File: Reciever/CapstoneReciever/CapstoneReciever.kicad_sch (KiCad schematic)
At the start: 70 parts, among them J1 Conn_01x04, J2 Conn_01x04, J3 Sol1Conn, J4 Sol2Conn, J5 Sol3Conn, J6 Sol4Conn, Q1 CSD18502Q5B, Q2 CSD18502Q5B, Q3 CSD18540Q5B, Q4 CSD18540Q5B, Q5 CSD18540Q5B, Q6 CSD18540Q5B, U1 LM73606RNPR, U2 TPS552882RPMR, U3 ESP32-WROOM-32UE

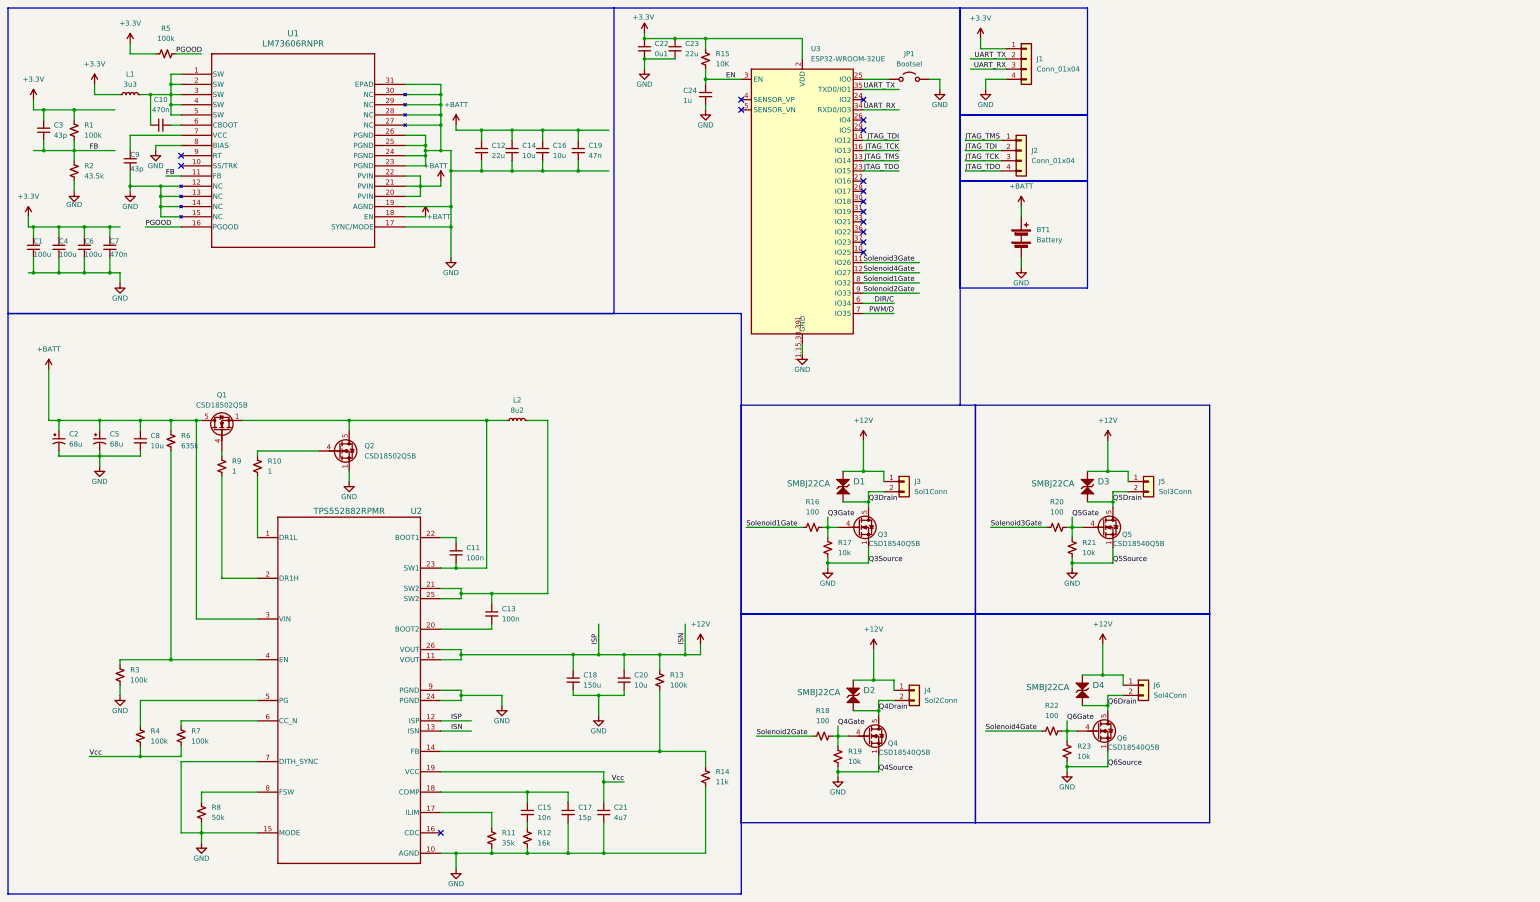
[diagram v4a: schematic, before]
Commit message: Removed convoluted battery power routing in exchange of DIN mounted AC-DC converter and DC-DC converter inputs
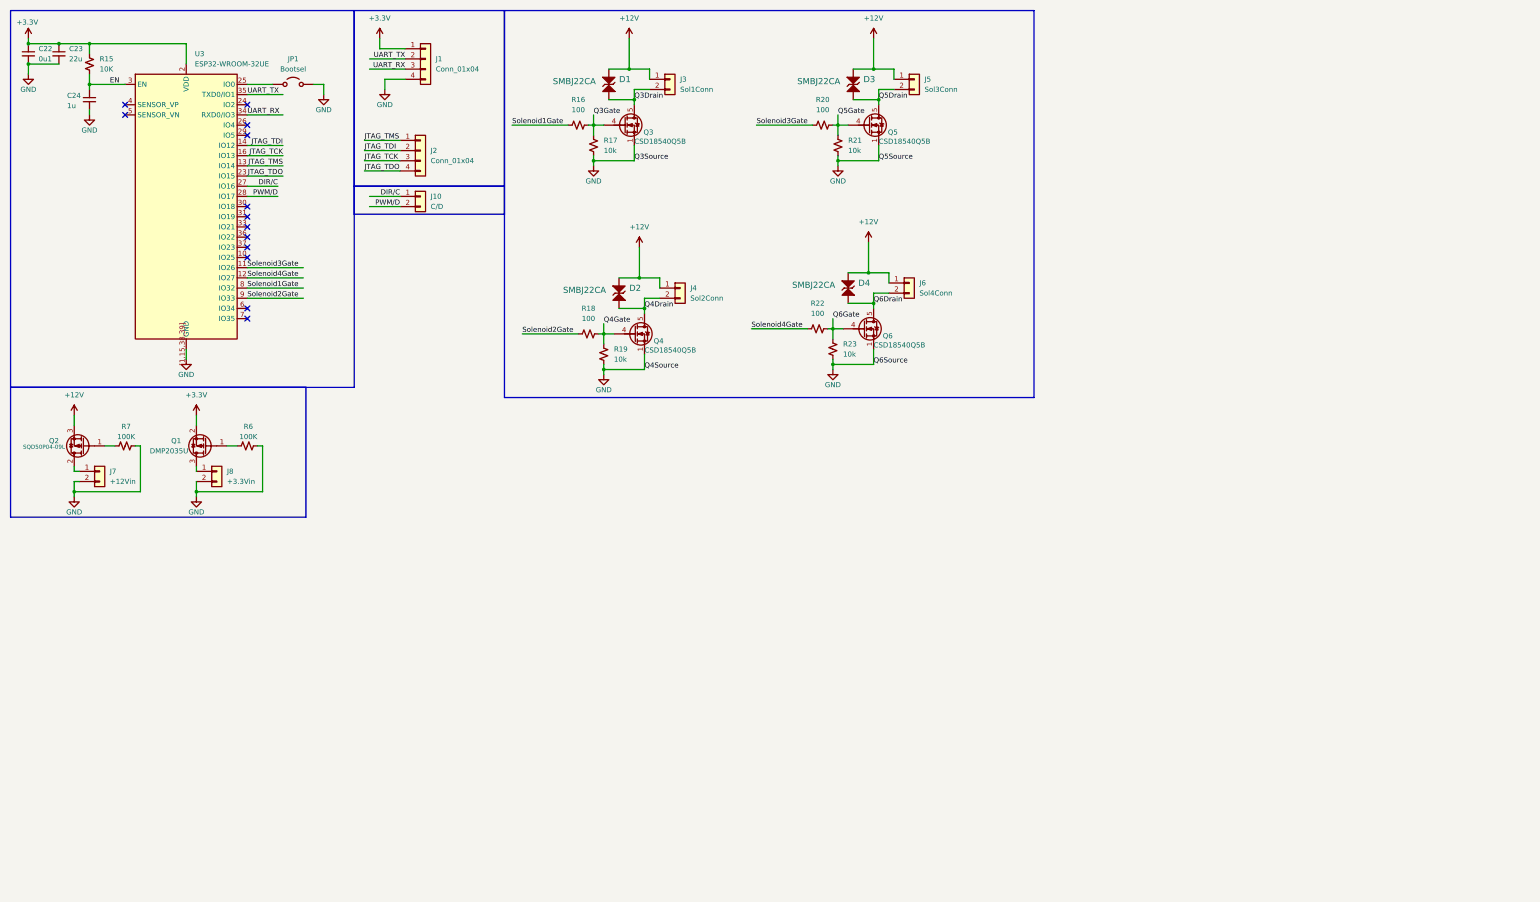
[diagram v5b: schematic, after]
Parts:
- removed BT1: Battery, TerminalBlock_CUI:TerminalBlock_CUI_TB007-508-02_1x02_P5.08mm_Horizontal, symbol Device:Battery
- removed C1, C4, C6: 100u, Capacitor_SMD:C_0603_1608Metric, symbol Device:C_Small
- removed C10, C7: 470n, Capacitor_SMD:C_0402_1005Metric, symbol Device:C_Small
- removed C11, C13: 100n, Capacitor_SMD:C_0402_1005Metric, symbol Device:C_Small
- removed C12: 22u, Capacitor_SMD:C_0603_1608Metric, symbol Device:C_Small
- removed C14, C16, C20, C8: 10u, Capacitor_SMD:C_0603_1608Metric, symbol Device:C_Small
- removed C15: 10n, Capacitor_SMD:C_0402_1005Metric, symbol Device:C_Small
- removed C17: 15p, Capacitor_SMD:C_0402_1005Metric, symbol Device:C_Small
- removed C18: 150u, Capacitor_SMD:C_0603_1608Metric, symbol Device:C_Small
- removed C19: 47n, Capacitor_SMD:C_0402_1005Metric, symbol Device:C_Small
- removed C2, C5: 68u, Capacitor_SMD:C_0603_1608Metric, symbol Device:C_Polarized_Small_US
- removed C21: 4u7, Capacitor_SMD:C_0603_1608Metric, symbol Device:C_Small
- removed C3, C9: 43p, Capacitor_SMD:C_0402_1005Metric, symbol Device:C_Small
- removed L1: 3u3, Capacitor_SMD:C_0603_1608Metric, symbol Device:L_Small
- removed L2: 8u2, Capacitor_SMD:C_0603_1608Metric, symbol Device:L_Small
- removed Q1, Q2: CSD18502Q5B, Package_TO_SOT_SMD:TDSON-8-1, symbol Transistor_FET:CSD18502Q5B
- removed R1, R13, R3, R4, R5: 100k, Resistor_SMD:R_0603_1608Metric, symbol Device:R_Small_US
- removed R10, R9: 1, Resistor_SMD:R_0603_1608Metric, symbol Device:R_Small_US
- removed R11: 35k, Resistor_SMD:R_0603_1608Metric, symbol Device:R_Small_US
- removed R12: 16k, Resistor_SMD:R_0603_1608Metric, symbol Device:R_Small_US
- removed R14: 11k, Resistor_SMD:R_0603_1608Metric, symbol Device:R_Small_US
- removed R2: 43.5k, Resistor_SMD:R_0603_1608Metric, symbol Device:R_Small_US
- removed R8: 50k, Resistor_SMD:R_0603_1608Metric, symbol Device:R_Small_US
- removed U1: LM73606RNPR, footprints2:RNP30_TEX, symbol LM73606:LM73606RNPR
- removed U2: TPS552882RPMR, footprints2:RPM0026A-MFG, symbol TPS552882RPMR:TPS552882RPMR
- added J10: C/D, TerminalBlock_CUI:TerminalBlock_CUI_TB007-508-02_1x02_P5.08mm_Horizontal, symbol Connector_Generic:Conn_01x02
- added J7: +12Vin, TerminalBlock_CUI:TerminalBlock_CUI_TB007-508-02_1x02_P5.08mm_Horizontal, symbol Connector_Generic:Conn_01x02
- added J8: +3.3Vin, TerminalBlock_CUI:TerminalBlock_CUI_TB007-508-02_1x02_P5.08mm_Horizontal, symbol Connector_Generic:Conn_01x02
- added Q1: DMP2035U, Package_TO_SOT_SMD:SOT-23, symbol Transistor_FET:DMP3099L
- added Q2: SQD50P04-09L, Package_TO_SOT_SMD:TO-252-3_TabPin2, symbol Transistor_FET:Q_PMOS_GDS
- R6: value 635k -> 100K
- R7: value 100k -> 100K
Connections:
- net Vcc is gone; now on net GND: R7.2
- net +12V: now also Q2.3 (S)
- net +3.3V: now also Q1.2 (S)
- net DIR/C: now also U3.27 (IO16), J10.1 (Pin_1); no longer U3.6 (IO34)
- net GND: now also R6.2, J7.2 (Pin_2), J8.2 (Pin_2)
- net PWM/D: now also U3.28 (IO17), J10.2 (Pin_2); no longer U3.7 (IO35)
- net at R7.1: now also Q2.1 (G)
- net +BATT: no longer names the net of R6.1
- net +BATT: now also Q1.1 (G)
- new net: J8.1 (Pin_1), Q1.3 (D)
- new net: J7.1 (Pin_1), Q2.2 (D)
- no-connect marks 16 -> 13
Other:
- moved on the sheet: C22, C23, C24, D1, D2, D3, D4, J1, J2, J3, J4, J5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

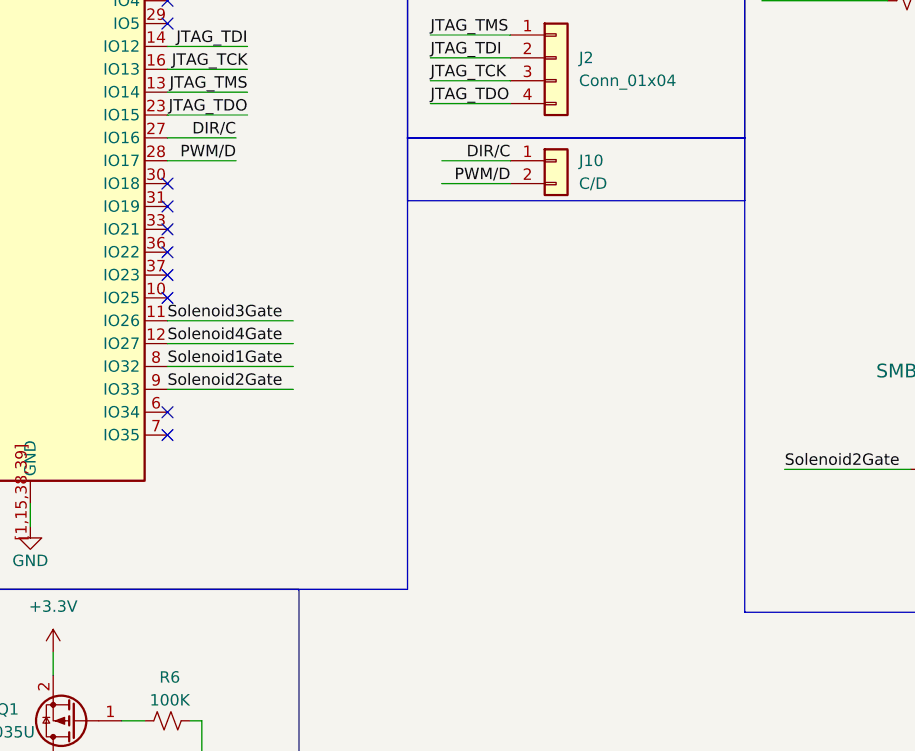
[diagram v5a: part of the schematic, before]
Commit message: Added in the solenoid labels, started implementing the endstops. Endstops need pull ups and should be set up for normally closed instead of open for fault protection.
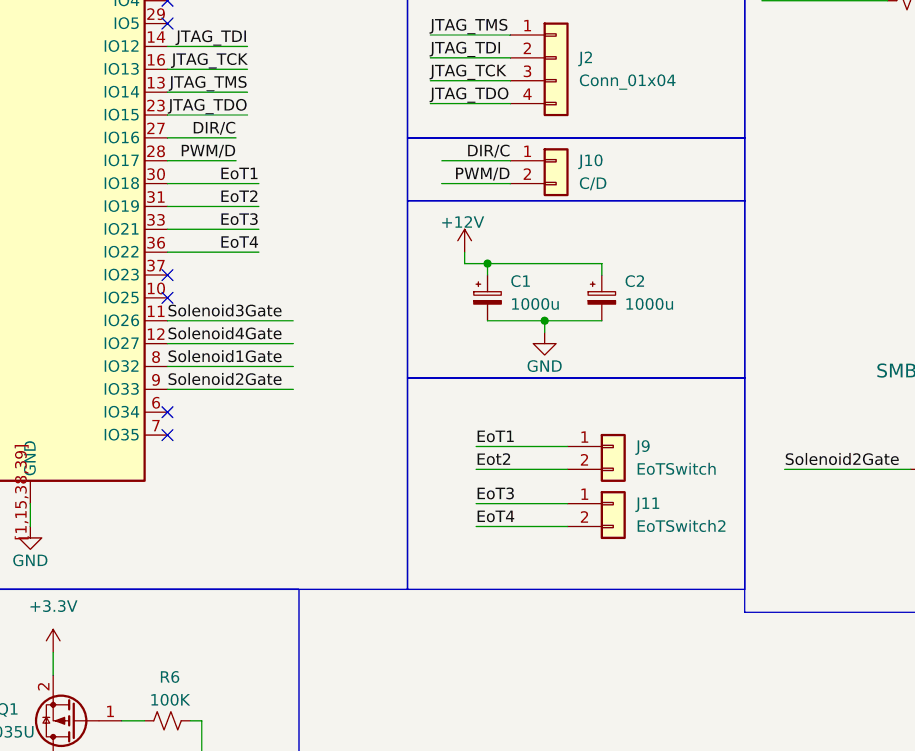
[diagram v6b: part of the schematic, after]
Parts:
- added C1, C2: 1000u, symbol Device:C_Polarized_Small
- added J11: EoTSwitch2, TerminalBlock_CUI:TerminalBlock_CUI_TB007-508-02_1x02_P5.08mm_Horizontal, symbol Connector_Generic:Conn_01x02
- added J9: EoTSwitch, TerminalBlock_CUI:TerminalBlock_CUI_TB007-508-02_1x02_P5.08mm_Horizontal, symbol Connector_Generic:Conn_01x02
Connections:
- net +12V: now also C1.1, C2.1
- net GND: now also C1.2, C2.2
- net EoT1: now reaches U3.30 (IO18)
- net EoT1: now also J9.1 (Pin_1)
- net EoT2: now reaches U3.31 (IO19)
- net EoT3: now reaches U3.33 (IO21)
- net EoT3: now also J11.1 (Pin_1)
- net EoT4: now reaches U3.36 (IO22)
- net EoT4: now also J11.2 (Pin_2)
- new net Eot2: J9.2 (Pin_2)
- no-connect marks 13 -> 9

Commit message: Finished routing End of Travel microswitch terminal blocks
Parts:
- C1, C2: footprint (none) -> Capacitor_SMD:CP_Elec_10x14.3
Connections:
- net Eot2 is gone; now on net EoT2: J9.2 (Pin_2)
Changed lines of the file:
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@@
 		)
 	)
-	(label "Eot2"
+	(label "EoT2"
 		(at 105.41 92.71 0)
 		(effects
@@
 			)
 		)
-		(property "Footprint" ""
+		(property "Footprint" "Capacitor_SMD:CP_Elec_10x14.3"
 			(at 119.38 73.66 0)
 			(hide yes)
@@
 			)
 		)
-		(property "Footprint" ""
+		(property "Footprint" "Capacitor_SMD:CP_Elec_10x14.3"
 			(at 106.68 73.66 0)
 			(hide yes)
